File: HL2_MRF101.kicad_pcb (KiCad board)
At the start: 4 copper layers, 149.9 x 100 mm, 219 parts, among them J1 Antenna, J10 DB1, J2 HL2, J3 RF3, J4 RF1, J5 RCJ-041, J6 50VDC, J7 12V, J8 Fan, J9 HL2_12V, K1 AXICOM D2N, K10 AXICOM D2N, K11 EC2-3NU, K12 AXICOM D2N, K13 EC2-3NU, K2 AXICOM D2N, K3 AXICOM D2N, K4 AXICOM D2N, K5 AXICOM D2N, K6 AXICOM D2N, K7 AXICOM D2N, K8 AXICOM D2N, K9 AXICOM D2N, Q1 MRF101AN, Q2 2N7002, Q3 IRLML6402, Q4 DTC144E, T1 Coupler, T2 Coupler, T3 744851330, U1 MCP6282E/MS, U2 MAX11645, U3 MCP23008, U4 ULN2003, U5 LM35-NEB, U6 MCP4561, U7 INA193

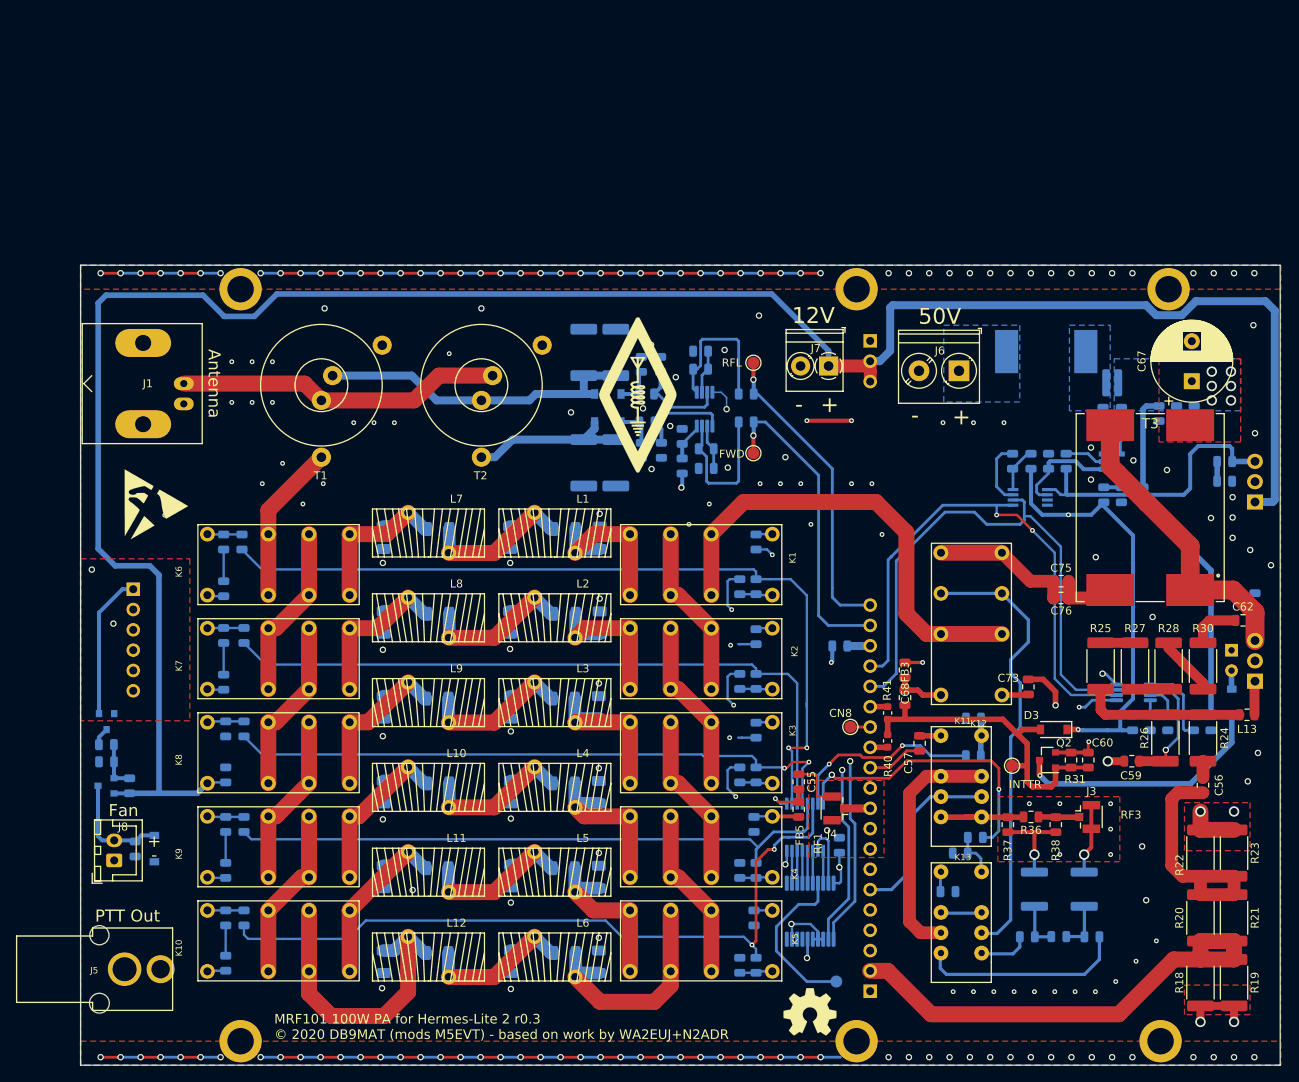
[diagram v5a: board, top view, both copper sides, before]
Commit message: Cleaned up silk screen
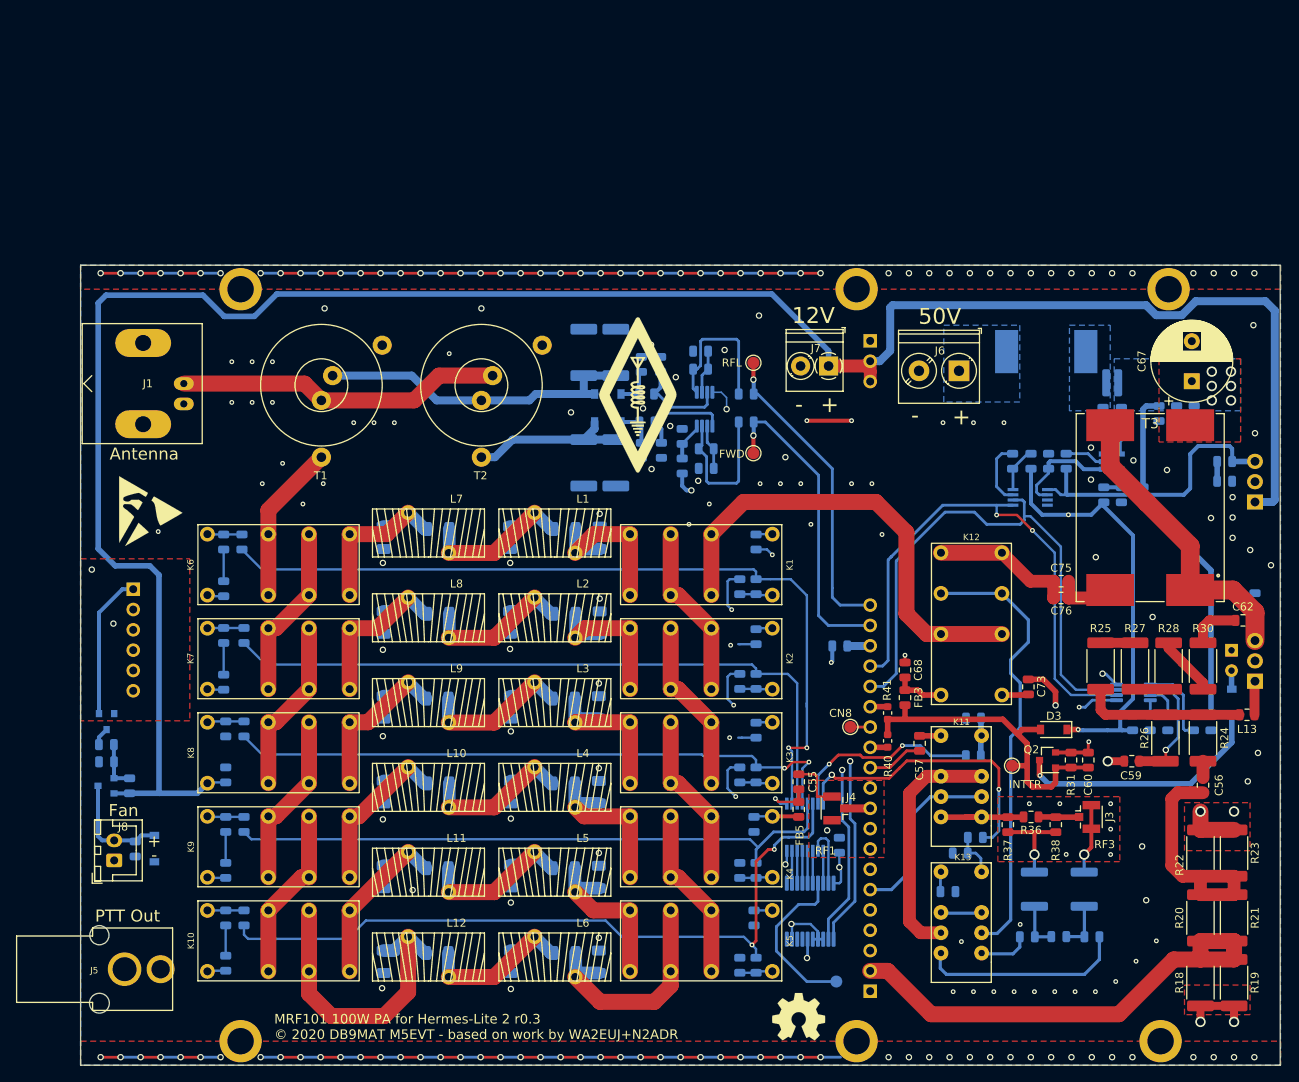
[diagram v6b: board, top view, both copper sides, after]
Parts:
- moved REF** 1.54 mm to (159.8, 133.9)
- moved REF** 1.23 mm to (159.8, 133.9)
- moved REF** 1.10 mm to (78.8, 70.8)
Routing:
- net GND: track 308.7 -> 307.4 mm, vias 222 -> 224
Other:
- board text added: "MRF101 100W PA for Hermes-Lite 2 r0.3 © 2020 DB9MAT M5EVT - based on work by WA2EUJ+N2ADR"
- board text removed: "MRF101 100W PA for Hermes-Lite 2 r0.3 © 2020 DB9MAT (mods M5EVT) - based on work by WA2EUJ+N2ADR"
